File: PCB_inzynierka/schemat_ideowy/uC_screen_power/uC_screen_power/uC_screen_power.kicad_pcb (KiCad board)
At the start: 4 copper layers, 100 x 100 mm, 17 parts, among them J1 Barrel_Jack_Switch, J2 Conn_01x04_Pin, J3 Conn_01x04_Pin, J4 Conn_01x04_Pin, J5 Conn_01x04_Pin, SW73 SW_DPST, SW74 SW_DPST, SW75 SW_DPST, SW76 SW_DPST, U10 TFT_320x240, U11 NUCLEO-F401RE

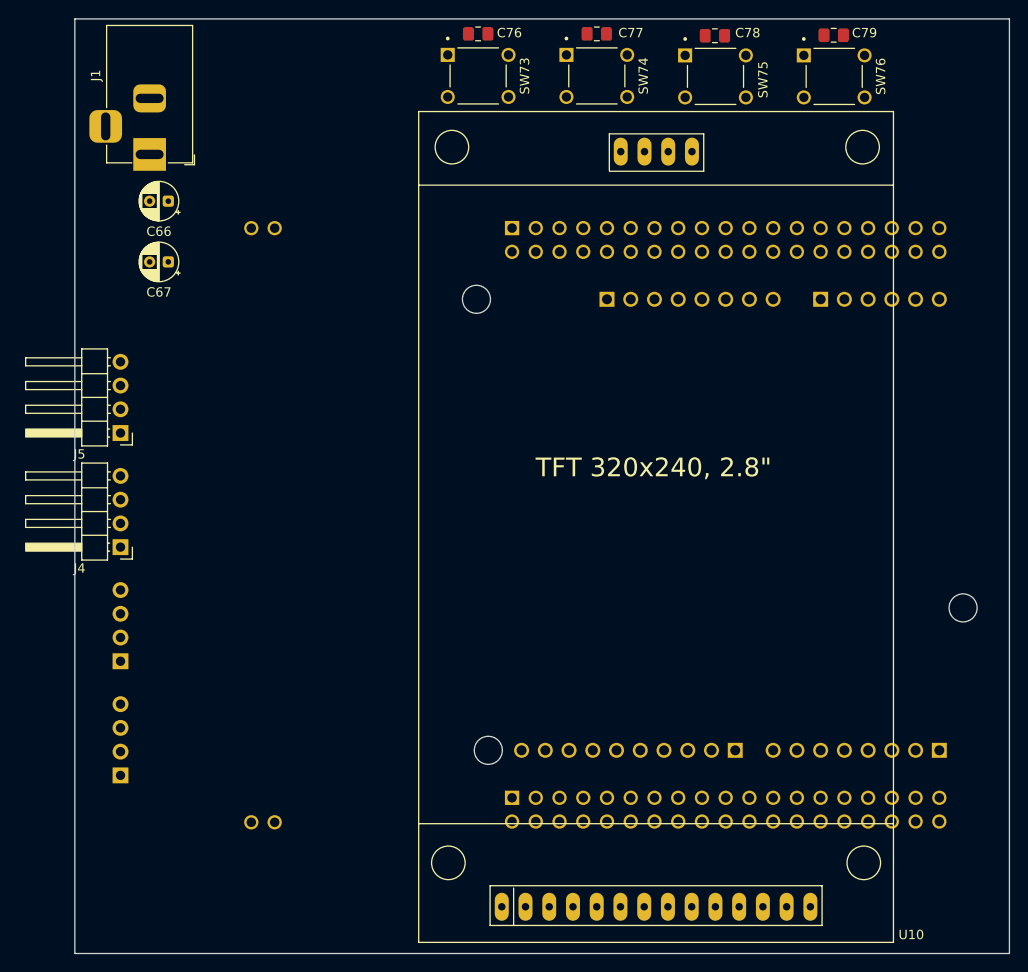
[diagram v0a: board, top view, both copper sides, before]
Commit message: obie plytki pcb przygotowane, schematy ideowe opisane
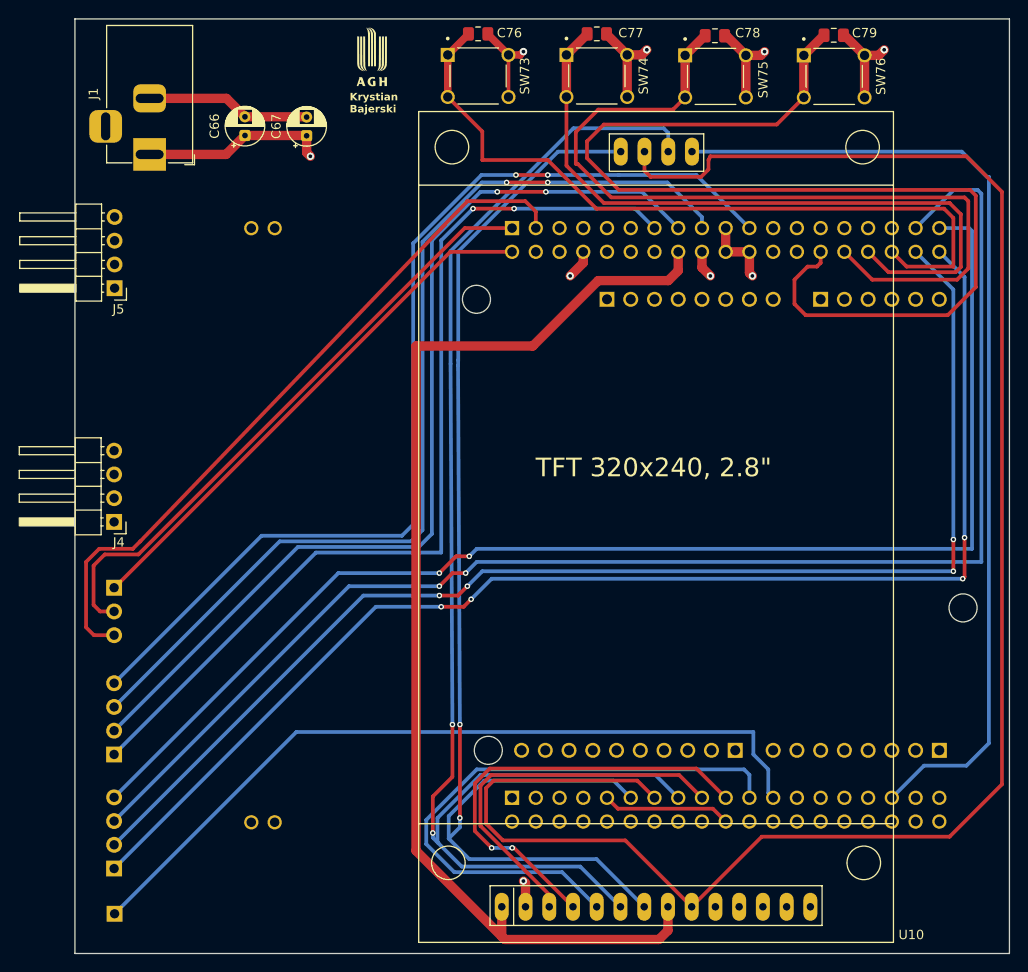
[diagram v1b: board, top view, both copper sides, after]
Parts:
- added G***: LOGO, LOGO, F.Cu at (83.8, 56.6)
- added J6: Conn_01x03_Pin, Connector_PinHeader_2.54mm:PinHeader_1x03_P2.54mm_Vertical, B.Cu at (56.2, 113.4)
- added J7: Conn_01x01_Pin, Connector_PinHeader_2.54mm:PinHeader_1x01_P2.54mm_Vertical, B.Cu at (56.2, 148.2)
- C76, C77, C78, C79: value 10uF -> 100nF
- moved C67 20.0 mm to (76.8, 65.0), turned to 90 degrees
- moved J5 15.5 mm to (56.2, 81.3)
- moved C66 10.8 mm to (70.2, 65.0), turned to 90 degrees
- moved J2 9.99 mm to (56.2, 143.4)
- moved J3 9.99 mm to (56.2, 131.2)
- moved J4 2.79 mm to (56.2, 106.3)
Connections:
- C66 pad 1: GND -> +5V
- C66 pad 2: +5V -> GND
- C67 pad 1: GND -> +5V
- C67 pad 2: +5V -> GND
- U11 pad 10_23: /LED_IN -> /LED_OUT
- U11 pad 7_1: unconnected-(U11A-PC10-Pad7_1) -> /S0
- U11 pad 7_2: unconnected-(U11A-PC11-Pad7_2) -> /S1
- U11 pad 7_3: unconnected-(U11A-PC12-Pad7_3) -> /S2
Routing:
- net /MISO: track 0.00 -> 194.3 mm
- net /MUX_OUT_2: track 0.00 -> 152.6 mm, vias 0 -> 2
- net /MOSI: track 0.00 -> 149.1 mm, vias 0 -> 2
- net /MUX_OUT_3: track 0.00 -> 140.4 mm, vias 0 -> 2
- net /MUX_OUT_0: track 0.00 -> 139.8 mm, vias 0 -> 4
- net /MUX_OUT_1: track 0.00 -> 137.8 mm, vias 0 -> 4
- net /SCK: track 0.00 -> 133.3 mm, vias 0 -> 2
- net /VDD: track 0.00 -> 124.4 mm
- net GND: track 0.00 -> 122.2 mm, vias 0 -> 7
- net /SW4: track 0.00 -> 116.0 mm
- net /MUX_OUT_4: track 0.00 -> 110.5 mm, vias 0 -> 2
- net /MUX_OUT_7: track 0.00 -> 106.9 mm, vias 0 -> 2
- net /CS_SD: track 0.00 -> 106.3 mm
- net /MUX_OUT_6: track 0.00 -> 104.2 mm, vias 0 -> 2
- net /MUX_OUT_5: track 0.00 -> 102.4 mm, vias 0 -> 2
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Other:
- board text added: "Krystian Bajerski"

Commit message: pcb v1.0, przygotowane pliki do fabryki pcb, zamowienie zlozone, poprawa przelotek
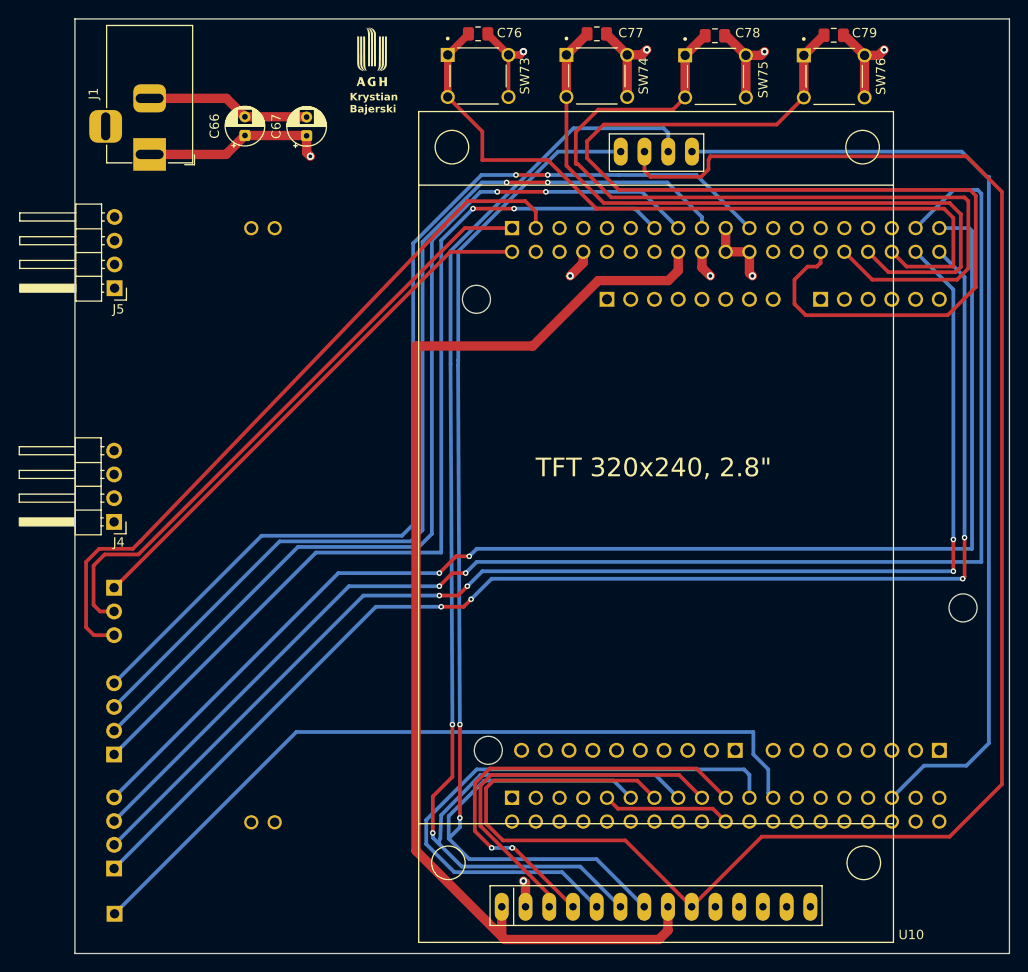
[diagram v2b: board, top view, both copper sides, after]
